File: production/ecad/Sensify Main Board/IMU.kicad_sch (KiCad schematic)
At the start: 5 parts, among them U5 LSM6DSOTR

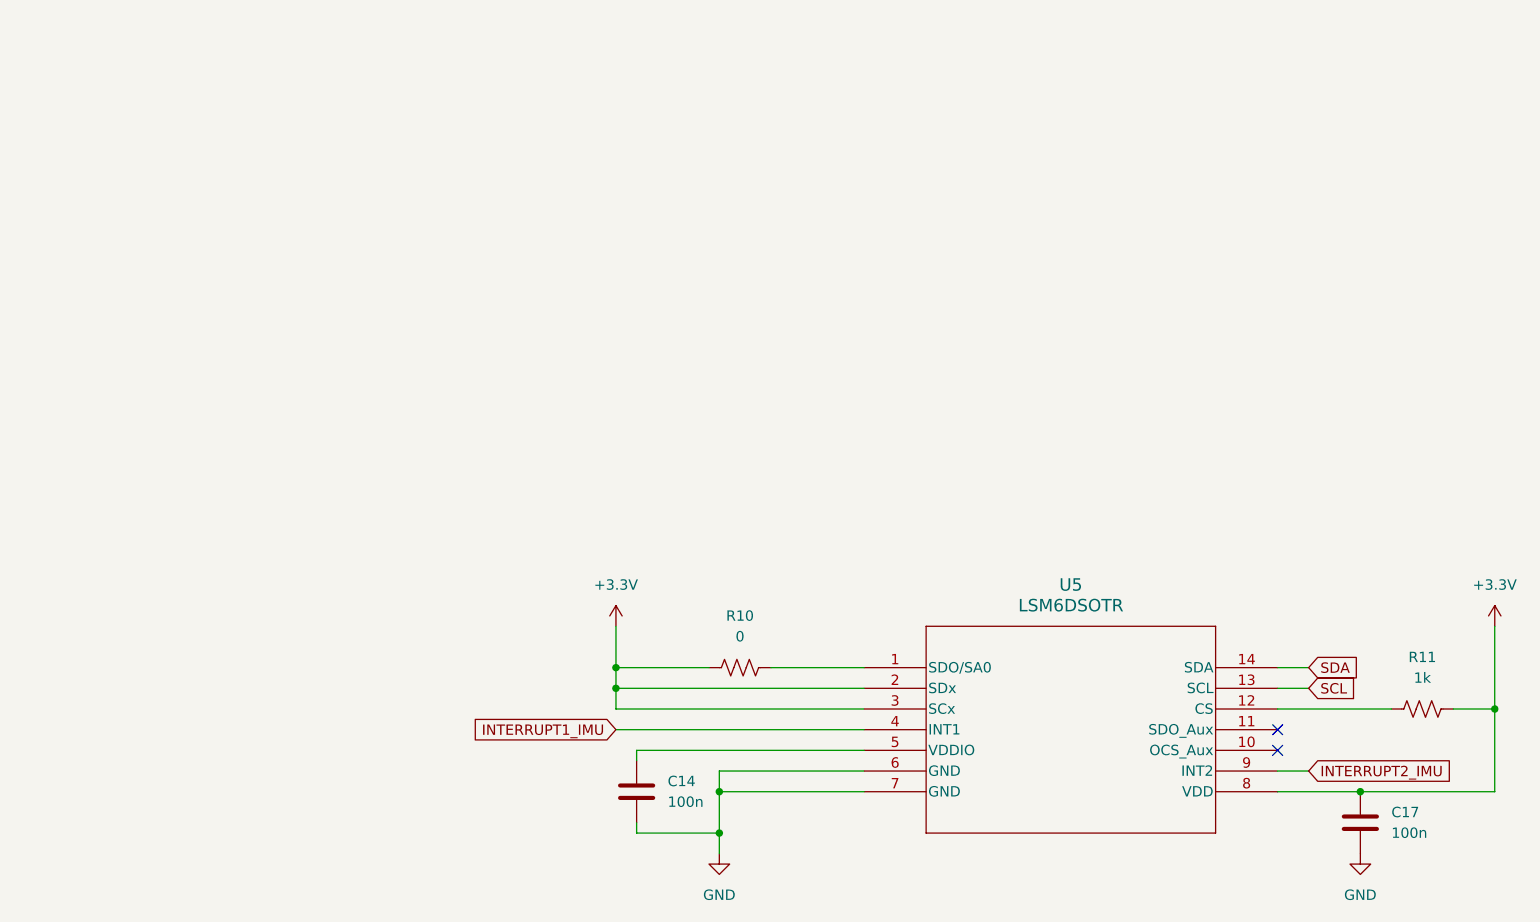
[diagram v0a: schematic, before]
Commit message: Net Changes
changed up some net names and added hierarchical labels
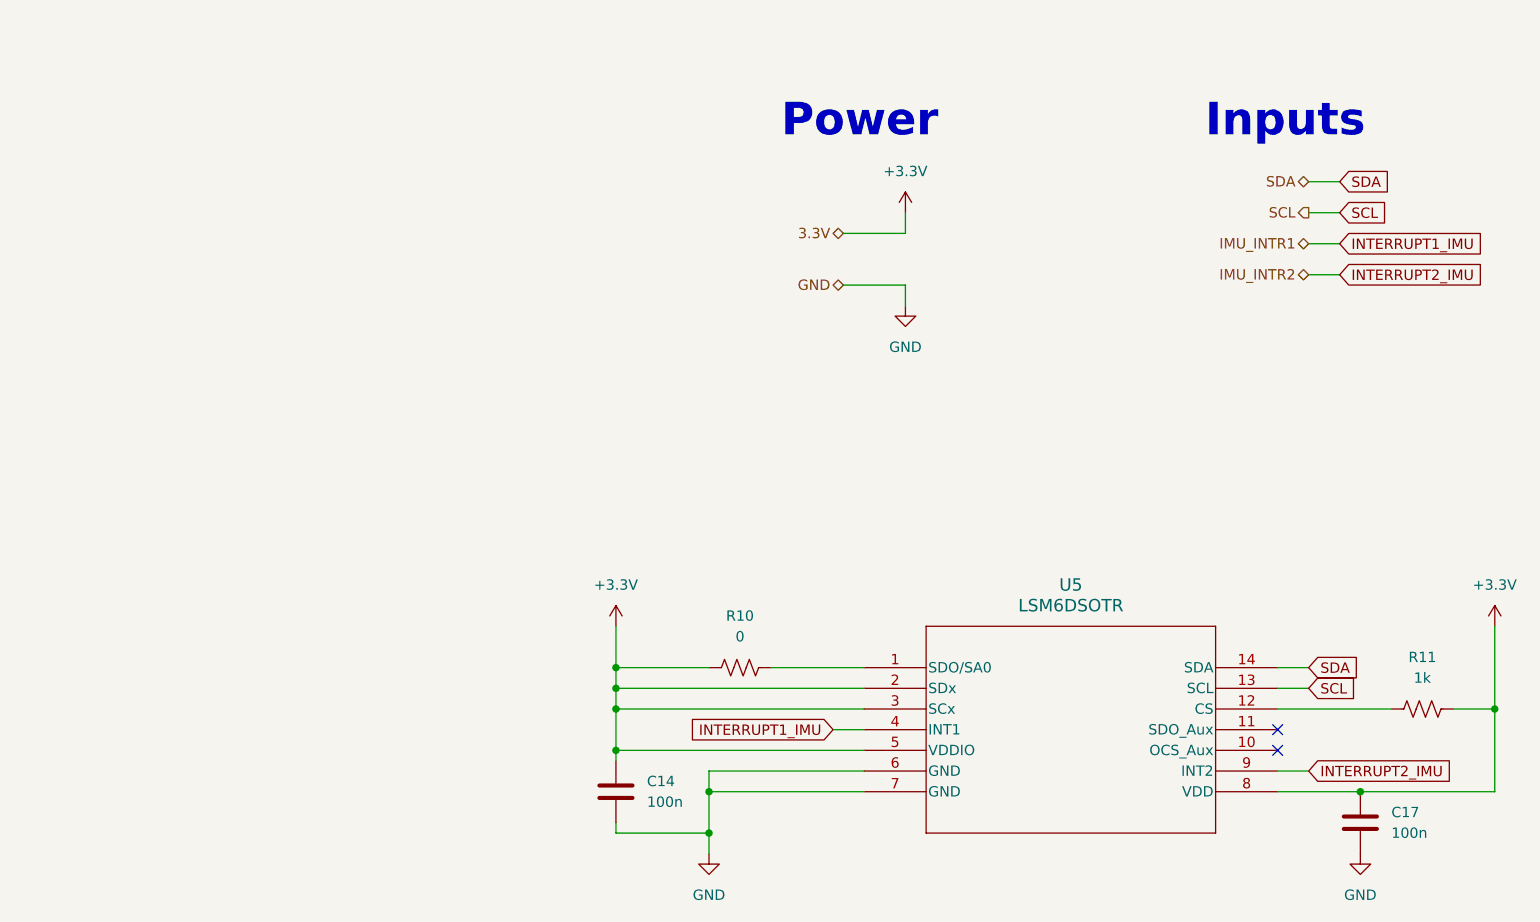
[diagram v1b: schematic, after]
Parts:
- C14, C17: footprint (none) -> Capacitor_SMD:C_0402_1005Metric
- R10, R11: footprint (none) -> Resistor_SMD:R_0402_1005Metric
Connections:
- net +3.3V: now also C14.1, U5.5 (VDDIO)
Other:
- note added: "Inputs"
- note added: "Power"
- moved on the sheet: C14

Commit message: Finished IMU, Haptics, MCU, and Root Page
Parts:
- added TP10, TP11: TestPoint, symbol Connector:TestPoint
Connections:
- net INTERRUPT1_IMU: now also TP10.1
- net INTERRUPT2_IMU: now also TP11.1
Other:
- note added: "IMU"
- note added: "TEST POINTS"
- moved on the sheet: C14, C17, R10, R11, U5

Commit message: Added Test Point footprints, fixed Haptics footprints, fixed IMU footprints
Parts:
- TP10, TP11: footprint (none) -> TestPoint:TestPoint_Pad_D2.0mm
- U?: renamed from U5; footprint SensifyIMU:IMU_LSM6DSOTR -> Sensify Footprints:IMU_LSM6DSOTR
- renumbered C17 to C?, C14 to C?, R10 to R?, R11 to R?
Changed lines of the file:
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@@
   (symbol (lib_id "power:+3.3V") (at 139.7 80.01 0) (unit 1)
     (in_bom yes) (on_board yes) (dnp no) (fields_autoplaced)
-    (property "Reference" "#PWR025" (at 139.7 83.82 0)
+    (property "Reference" "#PWR?" (at 139.7 83.82 0)
       (effects (font (size 1.27 1.27)) hide)
     )
@@
       (project "IMU"
         (path "/82d01545-2e1c-4e0d-b3d2-989b5d83c66c"
-          (reference "#PWR025") (unit 1)
-        )
-      )
-      (project "Sensify Main Board"
-        (path "/9a7ba7c3-7d28-4a83-bdbc-38fbff59fcbe/863c84cf-20d9-4517-8886-efede6184696"
-          (reference "#PWR025") (unit 1)
+          (reference "#PWR?") (unit 1)
+        )
+      )
+      (project "Sensify Main Board"
+        (path "/9a7ba7c3-7d28-4a83-bdbc-38fbff59fcbe/863c84cf-20d9-4517-8886-efede6184696"
+          (reference "#PWR0103") (unit 1)
         )
       )
@@
       (effects (font (size 1.27 1.27)) (justify left))
     )
-    (property "Footprint" "" (at 106.68 31.75 0)
+    (property "Footprint" "TestPoint:TestPoint_Pad_D2.0mm" (at 106.68 31.75 0)
       (effects (font (size 1.27 1.27)) hide)
     )
@@
   (symbol (lib_id "power:GND") (at 33.02 41.91 0) (unit 1)
     (in_bom yes) (on_board yes) (dnp no) (fields_autoplaced)
-    (property "Reference" "#PWR063" (at 33.02 48.26 0)
+    (property "Reference" "#PWR0100" (at 33.02 48.26 0)
       (effects (font (size 1.27 1.27)) hide)
     )
@@
       (project "Sensify Main Board"
         (path "/9a7ba7c3-7d28-4a83-bdbc-38fbff59fcbe/863c84cf-20d9-4517-8886-efede6184696"
-          (reference "#PWR063") (unit 1)
+          (reference "#PWR0100") (unit 1)
         )
       )
@@
   (symbol (lib_id "Device:C") (at 123.19 104.14 0) (unit 1)
     (in_bom yes) (on_board yes) (dnp no) (fields_autoplaced)
-    (property "Reference" "C17" (at 127 102.87 0)
+    (property "Reference" "C?" (at 127 102.87 0)
       (effects (font (size 1.27 1.27)) (justify left))
     )
@@
       (project "IMU"
         (path "/82d01545-2e1c-4e0d-b3d2-989b5d83c66c"
-          (reference "C17") (unit 1)
-        )
-      )
-      (project "Sensify Main Board"
-        (path "/9a7ba7c3-7d28-4a83-bdbc-38fbff59fcbe/863c84cf-20d9-4517-8886-efede6184696"
-          (reference "C17") (unit 1)
+          (reference "C?") (unit 1)
+        )
+      )
+      (project "Sensify Main Board"
+        (path "/9a7ba7c3-7d28-4a83-bdbc-38fbff59fcbe/863c84cf-20d9-4517-8886-efede6184696"
+          (reference "C42") (unit 1)
         )
       )
@@
   (symbol (lib_id "Device:R_US") (at 46.99 85.09 90) (unit 1)
     (in_bom yes) (on_board yes) (dnp no) (fields_autoplaced)
-    (property "Reference" "R10" (at 46.99 78.74 90)
+    (property "Reference" "R?" (at 46.99 78.74 90)
       (effects (font (size 1.27 1.27)))
     )
@@
       (project "IMU"
         (path "/82d01545-2e1c-4e0d-b3d2-989b5d83c66c"
-          (reference "R10") (unit 1)
-        )
-      )
-      (project "Sensify Main Board"
-        (path "/9a7ba7c3-7d28-4a83-bdbc-38fbff59fcbe/863c84cf-20d9-4517-8886-efede6184696"
-          (reference "R10") (unit 1)
+          (reference "R?") (unit 1)
+        )
+      )
+      (project "Sensify Main Board"
+        (path "/9a7ba7c3-7d28-4a83-bdbc-38fbff59fcbe/863c84cf-20d9-4517-8886-efede6184696"
+          (reference "R44") (unit 1)
         )
       )
@@
   (symbol (lib_id "power:GND") (at 43.18 107.95 0) (unit 1)
     (in_bom yes) (on_board yes) (dnp no) (fields_autoplaced)
-    (property "Reference" "#PWR023" (at 43.18 114.3 0)
+    (property "Reference" "#PWR?" (at 43.18 114.3 0)
       (effects (font (size 1.27 1.27)) hide)
     )
@@
       (project "IMU"
         (path "/82d01545-2e1c-4e0d-b3d2-989b5d83c66c"
-          (reference "#PWR023") (unit 1)
-        )
-      )
-      (project "Sensify Main Board"
-        (path "/9a7ba7c3-7d28-4a83-bdbc-38fbff59fcbe/863c84cf-20d9-4517-8886-efede6184696"
-          (reference "#PWR023") (unit 1)
+          (reference "#PWR?") (unit 1)
+        )
+      )
+      (project "Sensify Main Board"
+        (path "/9a7ba7c3-7d28-4a83-bdbc-38fbff59fcbe/863c84cf-20d9-4517-8886-efede6184696"
+          (reference "#PWR0101") (unit 1)
         )
       )
@@
   (symbol (lib_id "SensifyIMU:LSM6DSOTR") (at 62.23 85.09 0) (unit 1)
     (in_bom yes) (on_board yes) (dnp no) (fields_autoplaced)
-    (property "Reference" "U5" (at 87.63 74.93 0)
+    (property "Reference" "U?" (at 87.63 74.93 0)
       (effects (font (size 1.524 1.524)))
     )
@@
       (effects (font (size 1.524 1.524)))
     )
-    (property "Footprint" "SensifyIMU:IMU_LSM6DSOTR" (at 62.23 85.09 0)
+    (property "Footprint" "Sensify Footprints:IMU_LSM6DSOTR" (at 62.23 85.09 0)
       (effects (font (size 1.27 1.27) italic) hide)
     )
@@
       (project "IMU"
         (path "/82d01545-2e1c-4e0d-b3d2-989b5d83c66c"
-          (reference "U5") (unit 1)
-        )
-      )
-      (project "Sensify Main Board"
-        (path "/9a7ba7c3-7d28-4a83-bdbc-38fbff59fcbe/863c84cf-20d9-4517-8886-efede6184696"
-          (reference "U5") (unit 1)
+          (reference "U?") (unit 1)
+        )
+      )
+      (project "Sensify Main Board"
+        (path "/9a7ba7c3-7d28-4a83-bdbc-38fbff59fcbe/863c84cf-20d9-4517-8886-efede6184696"
+          (reference "U11") (unit 1)
         )
       )
@@
   (symbol (lib_id "Device:C") (at 31.75 100.33 0) (unit 1)
     (in_bom yes) (on_board yes) (dnp no) (fields_autoplaced)
-    (property "Reference" "C14" (at 35.56 99.06 0)
+    (property "Reference" "C?" (at 35.56 99.06 0)
       (effects (font (size 1.27 1.27)) (justify left))
     )
@@
       (project "IMU"
         (path "/82d01545-2e1c-4e0d-b3d2-989b5d83c66c"
-          (reference "C14") (unit 1)
-        )
-      )
-      (project "Sensify Main Board"
-        (path "/9a7ba7c3-7d28-4a83-bdbc-38fbff59fcbe/863c84cf-20d9-4517-8886-efede6184696"
-          (reference "C14") (unit 1)
+          (reference "C?") (unit 1)
+        )
+      )
+      (project "Sensify Main Board"
+        (path "/9a7ba7c3-7d28-4a83-bdbc-38fbff59fcbe/863c84cf-20d9-4517-8886-efede6184696"
+          (reference "C41") (unit 1)
         )
       )
@@
   (symbol (lib_id "power:+3.3V") (at 33.02 30.48 0) (unit 1)
     (in_bom yes) (on_board yes) (dnp no) (fields_autoplaced)
-    (property "Reference" "#PWR062" (at 33.02 34.29 0)
+    (property "Reference" "#PWR099" (at 33.02 34.29 0)
       (effects (font (size 1.27 1.27)) hide)
     )
@@
       (project "Sensify Main Board"
         (path "/9a7ba7c3-7d28-4a83-bdbc-38fbff59fcbe/863c84cf-20d9-4517-8886-efede6184696"
-          (reference "#PWR062") (unit 1)
+          (reference "#PWR099") (unit 1)
         )
       )
@@
   (symbol (lib_id "power:+3.3V") (at 31.75 80.01 0) (unit 1)
     (in_bom yes) (on_board yes) (dnp no) (fields_autoplaced)
-    (property "Reference" "#PWR022" (at 31.75 83.82 0)
+    (property "Reference" "#PWR?" (at 31.75 83.82 0)
       (effects (font (size 1.27 1.27)) hide)
     )
@@
       (project "IMU"
         (path "/82d01545-2e1c-4e0d-b3d2-989b5d83c66c"
-          (reference "#PWR022") (unit 1)
-        )
-      )
-      (project "Sensify Main Board"
-        (path "/9a7ba7c3-7d28-4a83-bdbc-38fbff59fcbe/863c84cf-20d9-4517-8886-efede6184696"
-          (reference "#PWR022") (unit 1)
+          (reference "#PWR?") (unit 1)
+        )
+      )
+      (project "Sensify Main Board"
+        (path "/9a7ba7c3-7d28-4a83-bdbc-38fbff59fcbe/863c84cf-20d9-4517-8886-efede6184696"
+          (reference "#PWR098") (unit 1)
         )
       )
@@
   (symbol (lib_id "Device:R_US") (at 130.81 90.17 90) (unit 1)
     (in_bom yes) (on_board yes) (dnp no) (fields_autoplaced)
-    (property "Reference" "R11" (at 130.81 83.82 90)
+    (property "Reference" "R?" (at 130.81 83.82 90)
       (effects (font (size 1.27 1.27)))
     )
@@
       (project "IMU"
         (path "/82d01545-2e1c-4e0d-b3d2-989b5d83c66c"
-          (reference "R11") (unit 1)
-        )
-      )
-      (project "Sensify Main Board"
-        (path "/9a7ba7c3-7d28-4a83-bdbc-38fbff59fcbe/863c84cf-20d9-4517-8886-efede6184696"
-          (reference "R11") (unit 1)
+          (reference "R?") (unit 1)
+        )
+      )
+      (project "Sensify Main Board"
+        (path "/9a7ba7c3-7d28-4a83-bdbc-38fbff59fcbe/863c84cf-20d9-4517-8886-efede6184696"
+          (reference "R45") (unit 1)
         )
       )
@@
       (effects (font (size 1.27 1.27)) (justify left))
     )
-    (property "Footprint" "" (at 139.7 31.75 0)
+    (property "Footprint" "TestPoint:TestPoint_Pad_D2.0mm" (at 139.7 31.75 0)
       (effects (font (size 1.27 1.27)) hide)
     )
@@
   (symbol (lib_id "power:GND") (at 123.19 107.95 0) (unit 1)
     (in_bom yes) (on_board yes) (dnp no) (fields_autoplaced)
-    (property "Reference" "#PWR024" (at 123.19 114.3 0)
+    (property "Reference" "#PWR?" (at 123.19 114.3 0)
       (effects (font (size 1.27 1.27)) hide)
     )
@@
       (project "IMU"
         (path "/82d01545-2e1c-4e0d-b3d2-989b5d83c66c"
-          (reference "#PWR024") (unit 1)
-        )
-      )
-      (project "Sensify Main Board"
-        (path "/9a7ba7c3-7d28-4a83-bdbc-38fbff59fcbe/863c84cf-20d9-4517-8886-efede6184696"
-          (reference "#PWR024") (unit 1)
-        )
-      )
+          (reference "#PWR?") (unit 1)
+        )
+      )
+      (project "Sensify Main Board"
+        (path "/9a7ba7c3-7d28-4a83-bdbc-38fbff59fcbe/863c84cf-20d9-4517-8886-efede6184696"
+          (reference "#PWR0102") (unit 1)
+        )
+      )

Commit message: Added Labels to Test Points
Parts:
- TP10: value TestPoint -> INTERRUPT1_IMU
- TP11: value TestPoint -> INTERRUPT2_IMU
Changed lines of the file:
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@@
       (project "Sensify Main Board"
         (path "/9a7ba7c3-7d28-4a83-bdbc-38fbff59fcbe/863c84cf-20d9-4517-8886-efede6184696"
-          (reference "#PWR0103") (unit 1)
+          (reference "#PWR0112") (unit 1)
         )
       )
@@
       (effects (font (size 1.27 1.27)) (justify left))
     )
-    (property "Value" "TestPoint" (at 104.14 29.718 0)
+    (property "Value" "INTERRUPT1_IMU" (at 104.14 29.718 0)
       (effects (font (size 1.27 1.27)) (justify left))
     )
@@
   (symbol (lib_id "power:GND") (at 33.02 41.91 0) (unit 1)
     (in_bom yes) (on_board yes) (dnp no) (fields_autoplaced)
-    (property "Reference" "#PWR0100" (at 33.02 48.26 0)
+    (property "Reference" "#PWR0109" (at 33.02 48.26 0)
       (effects (font (size 1.27 1.27)) hide)
     )
@@
       (project "Sensify Main Board"
         (path "/9a7ba7c3-7d28-4a83-bdbc-38fbff59fcbe/863c84cf-20d9-4517-8886-efede6184696"
-          (reference "#PWR0100") (unit 1)
+          (reference "#PWR0109") (unit 1)
         )
       )
@@
       (project "Sensify Main Board"
         (path "/9a7ba7c3-7d28-4a83-bdbc-38fbff59fcbe/863c84cf-20d9-4517-8886-efede6184696"
-          (reference "C42") (unit 1)
+          (reference "C39") (unit 1)
         )
       )
@@
       (project "Sensify Main Board"
         (path "/9a7ba7c3-7d28-4a83-bdbc-38fbff59fcbe/863c84cf-20d9-4517-8886-efede6184696"
-          (reference "R44") (unit 1)
+          (reference "R47") (unit 1)
         )
       )
@@
       (project "Sensify Main Board"
         (path "/9a7ba7c3-7d28-4a83-bdbc-38fbff59fcbe/863c84cf-20d9-4517-8886-efede6184696"
-          (reference "#PWR0101") (unit 1)
+          (reference "#PWR0110") (unit 1)
         )
       )
@@
       (project "Sensify Main Board"
         (path "/9a7ba7c3-7d28-4a83-bdbc-38fbff59fcbe/863c84cf-20d9-4517-8886-efede6184696"
-          (reference "C41") (unit 1)
+          (reference "C38") (unit 1)
         )
       )
@@
   (symbol (lib_id "power:+3.3V") (at 33.02 30.48 0) (unit 1)
     (in_bom yes) (on_board yes) (dnp no) (fields_autoplaced)
-    (property "Reference" "#PWR099" (at 33.02 34.29 0)
+    (property "Reference" "#PWR0108" (at 33.02 34.29 0)
       (effects (font (size 1.27 1.27)) hide)
     )
@@
       (project "Sensify Main Board"
         (path "/9a7ba7c3-7d28-4a83-bdbc-38fbff59fcbe/863c84cf-20d9-4517-8886-efede6184696"
-          (reference "#PWR099") (unit 1)
+          (reference "#PWR0108") (unit 1)
         )
       )
@@
       (project "Sensify Main Board"
         (path "/9a7ba7c3-7d28-4a83-bdbc-38fbff59fcbe/863c84cf-20d9-4517-8886-efede6184696"
-          (reference "#PWR098") (unit 1)
+          (reference "#PWR0107") (unit 1)
         )
       )
@@
       (project "Sensify Main Board"
         (path "/9a7ba7c3-7d28-4a83-bdbc-38fbff59fcbe/863c84cf-20d9-4517-8886-efede6184696"
-          (reference "R45") (unit 1)
+          (reference "R48") (unit 1)
         )
       )
@@
       (effects (font (size 1.27 1.27)) (justify left))
     )
-    (property "Value" "TestPoint" (at 137.16 29.718 0)
+    (property "Value" "INTERRUPT2_IMU" (at 137.16 29.718 0)
       (effects (font (size 1.27 1.27)) (justify left))
     )
@@
       (project "Sensify Main Board"
         (path "/9a7ba7c3-7d28-4a83-bdbc-38fbff59fcbe/863c84cf-20d9-4517-8886-efede6184696"
-          (reference "#PWR0102") (unit 1)
-        )
-      )
+          (reference "#PWR0111") (unit 1)
+        )
+      )

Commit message: Added LCSC parts to KiCAD
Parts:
- C? (x2): LCSC (none) -> C2180807
- renumbered TP10 to TP20, TP11 to TP21

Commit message: added JLC part numbers to main board
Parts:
- R?: LCSC (none) -> C60485
- R?: LCSC (none) -> C226698
- U?: LCSC (none) -> C2655100
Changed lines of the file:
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@@
+      (effects (font (size 1.27 1.27)) hide)
+    )
+    (property "LCSC" "C60485" (at 46.99 85.09 0)
       (effects (font (size 1.27 1.27)) hide)
     )
@@
     (property "Datasheet" "https://www.st.com/resource/en/datasheet/lsm6dso.pdf" (at 62.23 85.09 0)
       (effects (font (size 1.27 1.27) italic) hide)
+    )
+    (property "LCSC" "C2655100" (at 62.23 85.09 0)
+      (effects (font (size 1.27 1.27)) hide)
     )
     (pin "4")
@@
       (effects (font (size 1.27 1.27)) hide)
     )
+    (property "LCSC" "C226698" (at 130.81 90.17 0)
+      (effects (font (size 1.27 1.27)) hide)
+    )
